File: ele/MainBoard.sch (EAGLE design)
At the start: 120 parts, among them IC1 MCP23017SP, IC2 74HC595D, IC3 74HC595D, X1 POWER_IN, X2 POWER_OUT

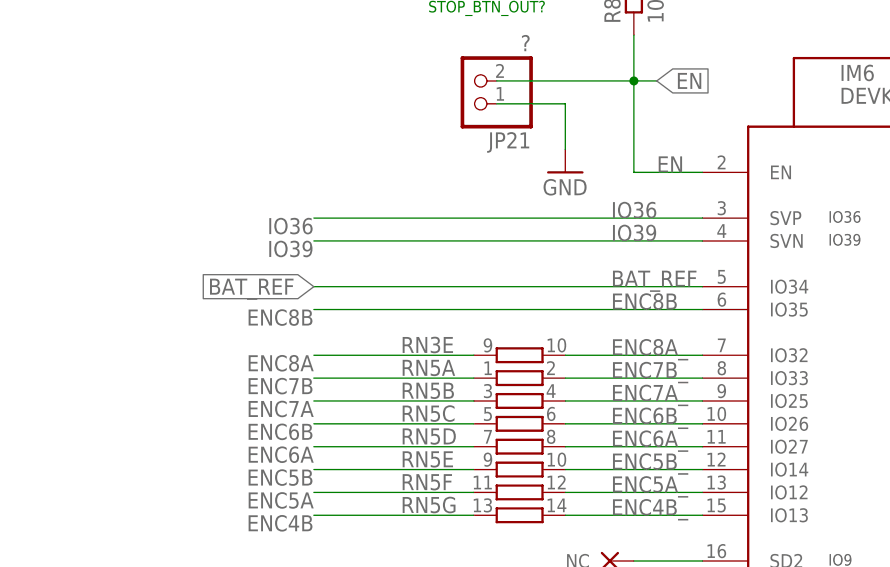
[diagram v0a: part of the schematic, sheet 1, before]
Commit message: ele: Fix typo in net name, move components around
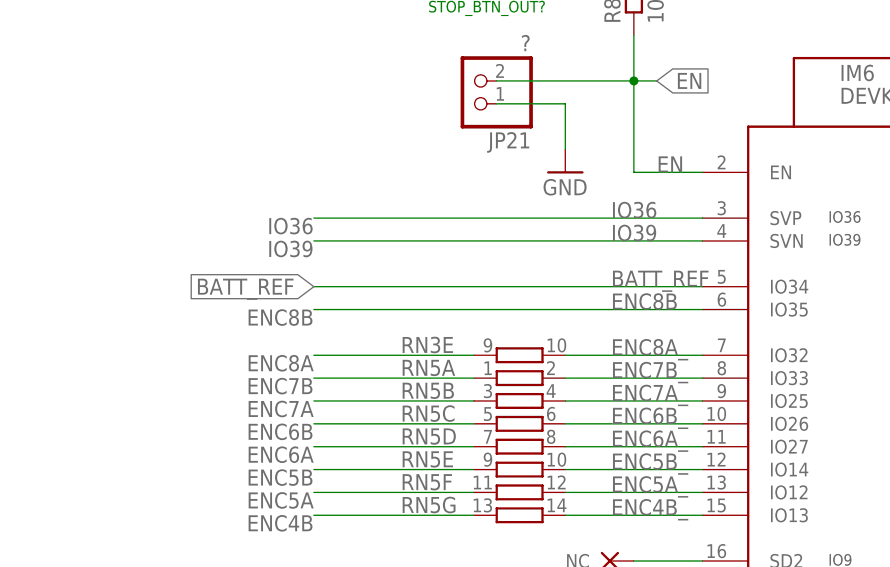
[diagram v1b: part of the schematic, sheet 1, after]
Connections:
- net BATT-ANODE renamed BATT_ANODE2
- net BAT_REF renamed BATT_REF
- removed net BAT_ANODE: Q3.D
- net BATT_ANODE: now also Q3.D
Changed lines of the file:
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@@
 <grid distance="0.1" unitdist="inch" unit="inch" style="lines" multiple="1" display="no" altdistance="0.01" altunitdist="inch" altunit="inch"/>
 <layers>
-<layer number="1" name="Top" color="4" fill="1" visible="yes" active="no"/>
-<layer number="2" name="Route2" color="1" fill="3" visible="yes" active="no"/>
-<layer number="3" name="Route3" color="4" fill="3" visible="yes" active="no"/>
-<layer number="4" name="Route4" color="1" fill="4" visible="yes" active="no"/>
-<layer number="5" name="Route5" color="4" fill="4" visible="yes" active="no"/>
-<layer number="6" name="Route6" color="1" fill="8" visible="yes" active="no"/>
-<layer number="7" name="Route7" color="4" fill="8" visible="yes" active="no"/>
-<layer number="8" name="Route8" color="1" fill="2" visible="yes" active="no"/>
-<layer number="9" name="Route9" color="4" fill="2" visible="yes" active="no"/>
-<layer number="10" name="Route10" color="1" fill="7" visible="yes" active="no"/>
-<layer number="11" name="Route11" color="4" fill="7" visible="yes" active="no"/>
-<layer number="12" name="Route12" color="1" fill="5" visible="yes" active="no"/>
-<layer number="13" name="Route13" color="4" fill="5" visible="yes" active="no"/>
-<layer number="14" name="Route14" color="1" fill="6" visible="yes" active="no"/>
-<layer number="15" name="Route15" color="4" fill="6" visible="yes" active="no"/>
-<layer number="16" name="Bottom" color="1" fill="1" visible="yes" active="no"/>
-<layer number="17" name="Pads" color="2" fill="1" visible="yes" active="no"/>
-<layer number="18" name="Vias" color="2" fill="1" visible="yes" active="no"/>
-<layer number="19" name="Unrouted" color="6" fill="1" visible="yes" active="no"/>
-<layer number="20" name="Dimension" color="24" fill="1" visible="yes" active="no"/>
-<layer number="21" name="tPlace" color="7" fill="1" visible="yes" active="no"/>
-<layer number="22" name="bPlace" color="7" fill="1" visible="yes" active="no"/>
-<layer number="23" name="tOrigins" color="15" fill="1" visible="yes" active="no"/>
-<layer number="24" name="bOrigins" color="15" fill="1" visible="yes" active="no"/>
-<layer number="25" name="tNames" color="7" fill="1" visible="yes" active="no"/>
-<layer number="26" name="bNames" color="7" fill="1" visible="yes" active="no"/>
-<layer number="27" name="tValues" color="7" fill="1" visible="yes" active="no"/>
-<layer number="28" name="bValues" color="7" fill="1" visible="yes" active="no"/>
+<layer number="1" name="Top" color="4" fill="1" visible="no" active="no"/>
+<layer number="2" name="Route2" color="1" fill="3" visible="no" active="no"/>
+<layer number="3" name="Route3" color="4" fill="3" visible="no" active="no"/>
+<layer number="4" name="Route4" color="1" fill="4" visible="no" active="no"/>
+<layer number="5" name="Route5" color="4" fill="4" visible="no" active="no"/>
+<layer number="6" name="Route6" color="1" fill="8" visible="no" active="no"/>
+<layer number="7" name="Route7" color="4" fill="8" visible="no" active="no"/>
+<layer number="8" name="Route8" color="1" fill="2" visible="no" active="no"/>
+<layer number="9" name="Route9" color="4" fill="2" visible="no" active="no"/>
+<layer number="10" name="Route10" color="1" fill="7" visible="no" active="no"/>
+<layer number="11" name="Route11" color="4" fill="7" visible="no" active="no"/>
+<layer number="12" name="Route12" color="1" fill="5" visible="no" active="no"/>
+<layer number="13" name="Route13" color="4" fill="5" visible="no" active="no"/>
+<layer number="14" name="Route14" color="1" fill="6" visible="no" active="no"/>
+<layer number="15" name="Route15" color="4" fill="6" visible="no" active="no"/>
+<layer number="16" name="Bottom" color="1" fill="1" visible="no" active="no"/>
+<layer number="17" name="Pads" color="2" fill="1" visible="no" active="no"/>
+<layer number="18" name="Vias" color="2" fill="1" visible="no" active="no"/>
+<layer number="19" name="Unrouted" color="6" fill="1" visible="no" active="no"/>
+<layer number="20" name="Dimension" color="24" fill="1" visible="no" active="no"/>
+<layer number="21" name="tPlace" color="7" fill="1" visible="no" active="no"/>
+<layer number="22" name="bPlace" color="7" fill="1" visible="no" active="no"/>
+<layer number="23" name="tOrigins" color="15" fill="1" visible="no" active="no"/>
+<layer number="24" name="bOrigins" color="15" fill="1" visible="no" active="no"/>
+<layer number="25" name="tNames" color="7" fill="1" visible="no" active="no"/>
+<layer number="26" name="bNames" color="7" fill="1" visible="no" active="no"/>
+<layer number="27" name="tValues" color="7" fill="1" visible="no" active="no"/>
+<layer number="28" name="bValues" color="7" fill="1" visible="no" active="no"/>
 <layer number="29" name="tStop" color="7" fill="3" visible="no" active="no"/>
 <layer number="30" name="bStop" color="7" fill="6" visible="no" active="no"/>
@@
 <layer number="35" name="tGlue" color="7" fill="4" visible="no" active="no"/>
 <layer number="36" name="bGlue" color="7" fill="5" visible="no" active="no"/>
-<layer number="37" name="tTest" color="7" fill="1" visible="yes" active="no"/>
-<layer number="38" name="bTest" color="7" fill="1" visible="yes" active="no"/>
+<layer number="37" name="tTest" color="7" fill="1" visible="no" active="no"/>
+<layer number="38" name="bTest" color="7" fill="1" visible="no" active="no"/>
 <layer number="39" name="tKeepout" color="4" fill="11" visible="no" active="no"/>
 <layer number="40" name="bKeepout" color="1" fill="11" visible="no" active="no"/>
@@
 <layer number="44" name="Drills" color="7" fill="1" visible="no" active="no"/>
 <layer number="45" name="Holes" color="7" fill="1" visible="no" active="no"/>
-<layer number="46" name="Milling" color="3" fill="1" visible="yes" active="no"/>
-<layer number="47" name="Measures" color="7" fill="1" visible="yes" active="no"/>
-<layer number="48" name="Document" color="7" fill="1" visible="yes" active="no"/>
-<layer number="49" name="Reference" color="7" fill="1" visible="yes" active="no"/>
-<layer number="50" name="dxf" color="7" fill="1" visible="yes" active="no"/>
-<layer number="51" name="tDocu" color="7" fill="1" visible="yes" active="no"/>
-<layer number="52" name="bDocu" color="7" fill="1" visible="yes" active="no"/>
-<layer number="53" name="tGND_GNDA" color="7" fill="9" visible="yes" active="no"/>
-<layer number="54" name="bGND_GNDA" color="1" fill="9" visible="yes" active="no"/>
-<layer number="55" name="tPotisk" color="7" fill="1" visible="yes" active="no"/>
-<layer number="56" name="wert" color="7" fill="1" visible="yes" active="no"/>
-<layer number="57" name="tCAD" color="7" fill="1" visible="yes" active="no"/>
-<layer number="58" name="bNC" color="7" fill="1" visible="yes" active="no"/>
-<layer number="59" name="tCarbon" color="7" fill="1" visible="yes" active="no"/>
-<layer number="60" name="bCarbon" color="7" fill="1" visible="yes" active="no"/>
-<layer number="61" name="stand" color="7" fill="1" visible="yes" active="no"/>
+<layer number="46" name="Milling" color="3" fill="1" visible="no" active="no"/>
+<layer number="47" name="Measures" color="7" fill="1" visible="no" active="no"/>
+<layer number="48" name="Document" color="7" fill="1" visible="no" active="no"/>
+<layer number="49" name="Reference" color="7" fill="1" visible="no" active="no"/>
+<layer number="50" name="dxf" color="7" fill="1" visible="no" active="no"/>
+<layer number="51" name="tDocu" color="7" fill="1" visible="no" active="no"/>
+<layer number="52" name="bDocu" color="7" fill="1" visible="no" active="no"/>
+<layer number="53" name="tGND_GNDA" color="7" fill="9" visible="no" active="no"/>
+<layer number="54" name="bGND_GNDA" color="1" fill="9" visible="no" active="no"/>
+<layer number="55" name="tPotisk" color="7" fill="1" visible="no" active="no"/>
+<layer number="56" name="wert" color="7" fill="1" visible="no" active="no"/>
+<layer number="57" name="tCAD" color="7" fill="1" visible="no" active="no"/>
+<layer number="58" name="bNC" color="7" fill="1" visible="no" active="no"/>
+<layer number="59" name="tCarbon" color="7" fill="1" visible="no" active="no"/>
+<layer number="60" name="bCarbon" color="7" fill="1" visible="no" active="no"/>
+<layer number="61" name="stand" color="7" fill="1" visible="no" active="no"/>
 <layer number="88" name="SimResults" color="9" fill="1" visible="yes" active="yes"/>
 <layer number="89" name="SimProbes" color="9" fill="1" visible="yes" active="yes"/>
@@
 </segment>
 </net>
-<net name="BAT_REF" class="0">
+<net name="BATT_REF" class="0">
 <segment>
 <label x="205.74" y="200.66" size="1.778" layer="95" rot="R180" xref="yes"/>
@@
 </segment>
 </net>
-<net name="BAT_REF" class="0">
+<net name="BATT_REF" class="0">
 <segment>
 <pinref part="R3" gate="G$1" pin="2"/>
@@
 <label x="127" y="193.04" size="1.778" layer="95"/>
 </segment>
+<segment>
+<pinref part="Q3" gate="G$1" pin="D"/>
+<wire x1="15.24" y1="182.88" x2="15.24" y2="177.8" width="0.1524" layer="91"/>
+<label x="15.24" y="177.8" size="1.778" layer="95" rot="R270"/>
+</segment>
 </net>
 <net name="N$4" class="0">
@@
 </segment>
 </net>
-<net name="BATT-ANODE" class="0">
+<net name="BATT_ANODE2" class="0">
 <segment>
 <pinref part="Q1" gate="G$1" pin="S"/>
@@
 </segment>
 </net>
-<net name="BAT_ANODE" class="0">
-<segment>
-<pinref part="Q3" gate="G$1" pin="D"/>
-<wire x1="15.24" y1="182.88" x2="15.24" y2="177.8" width="0.1524" layer="91"/>
-<label x="15.24" y="177.8" size="1.778" layer="95" rot="R270"/>
-</segment>
-</net>

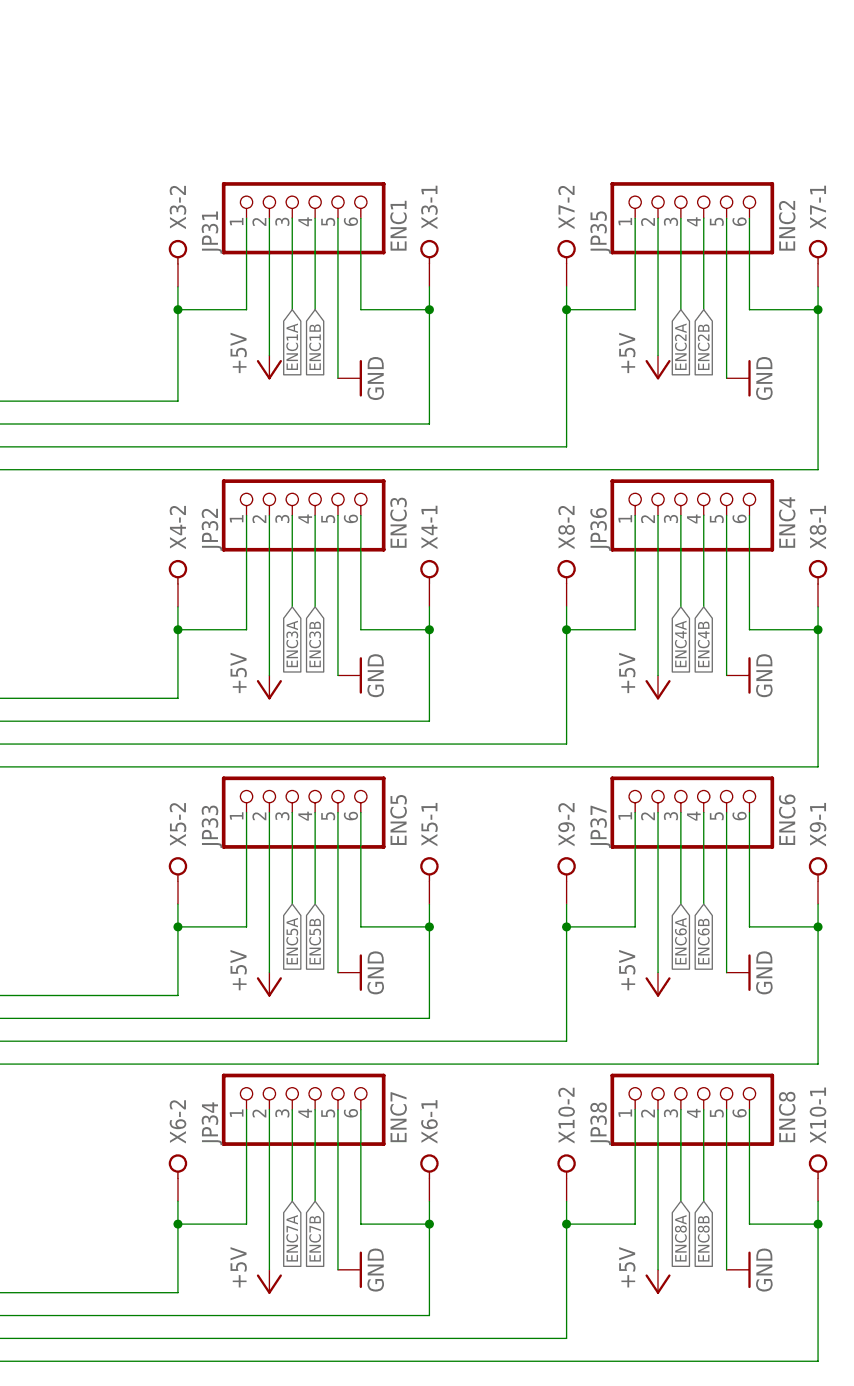
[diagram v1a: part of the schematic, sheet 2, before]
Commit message: ele: Create main power polygons, flip power connectors
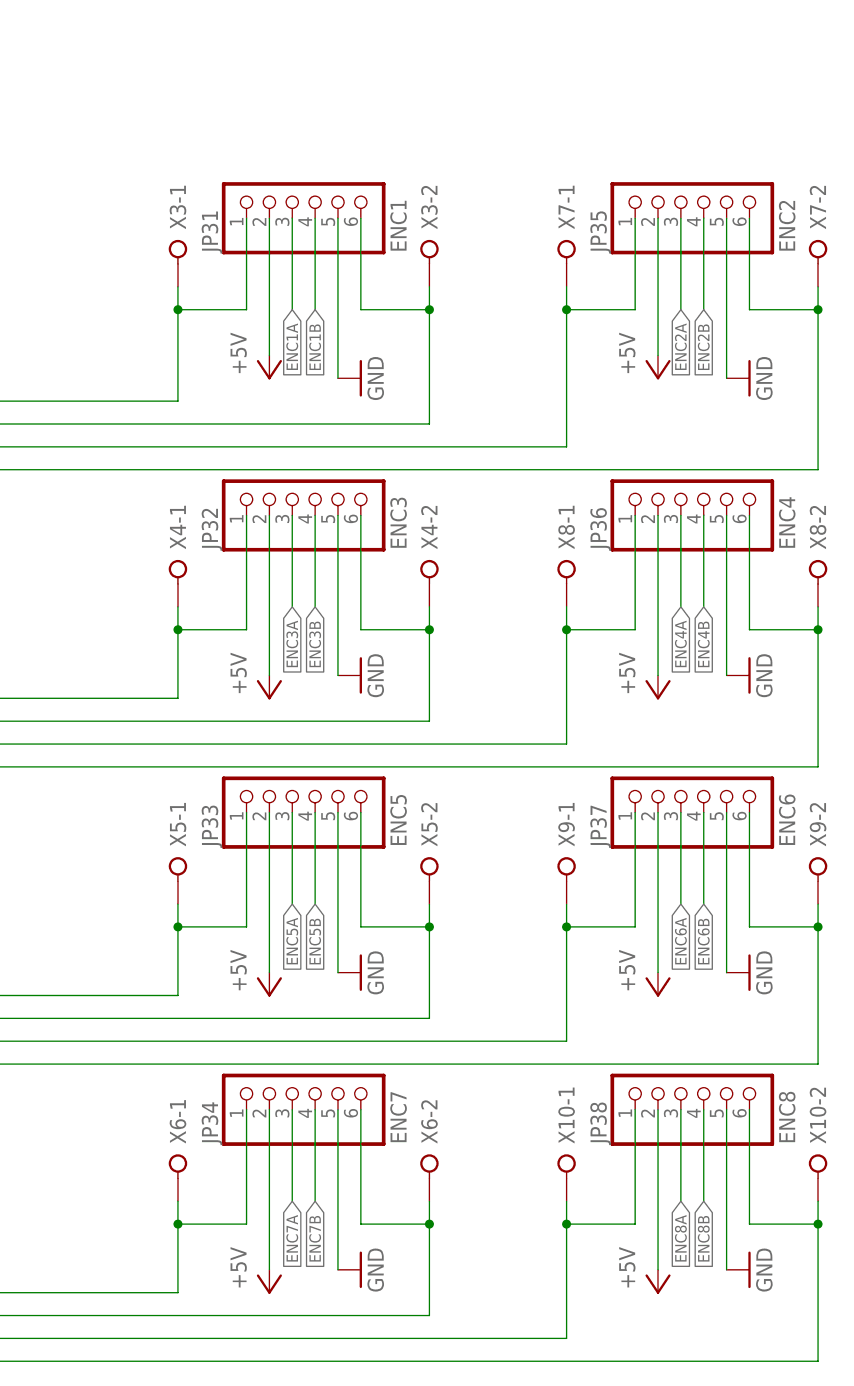
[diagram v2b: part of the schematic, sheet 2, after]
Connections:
- net IM10_O1: now also X6-1.KL; no longer X6-2.KL
- net IM10_O2: now also X6-2.KL; no longer X6-1.KL
- net IM10_O3: now also X10-1.KL; no longer X10-2.KL
- net IM10_O4: now also X10-2.KL; no longer X10-1.KL
- net IM7_O1: now also X3-1.KL; no longer X3-2.KL
- net IM7_O2: now also X3-2.KL; no longer X3-1.KL
- net IM7_O3: now also X7-1.KL; no longer X7-2.KL
- net IM7_O4: now also X7-2.KL; no longer X7-1.KL
- net IM8_O1: now also X4-1.KL; no longer X4-2.KL
- net IM8_O2: now also X4-2.KL; no longer X4-1.KL
- net IM8_O3: now also X8-1.KL; no longer X8-2.KL
- net IM8_O4: now also X8-2.KL; no longer X8-1.KL
- net IM9_O1: now also X5-1.KL; no longer X5-2.KL
- net IM9_O2: now also X5-2.KL; no longer X5-1.KL
- net IM9_O3: now also X9-1.KL; no longer X9-2.KL
- net IM9_O4: now also X9-2.KL; no longer X9-1.KL
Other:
- moved on the sheet: X10-1, X10-2, X3-1, X3-2, X4-1, X4-2, X5-1, X5-2, X6-1, X6-2, X7-1, X7-2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

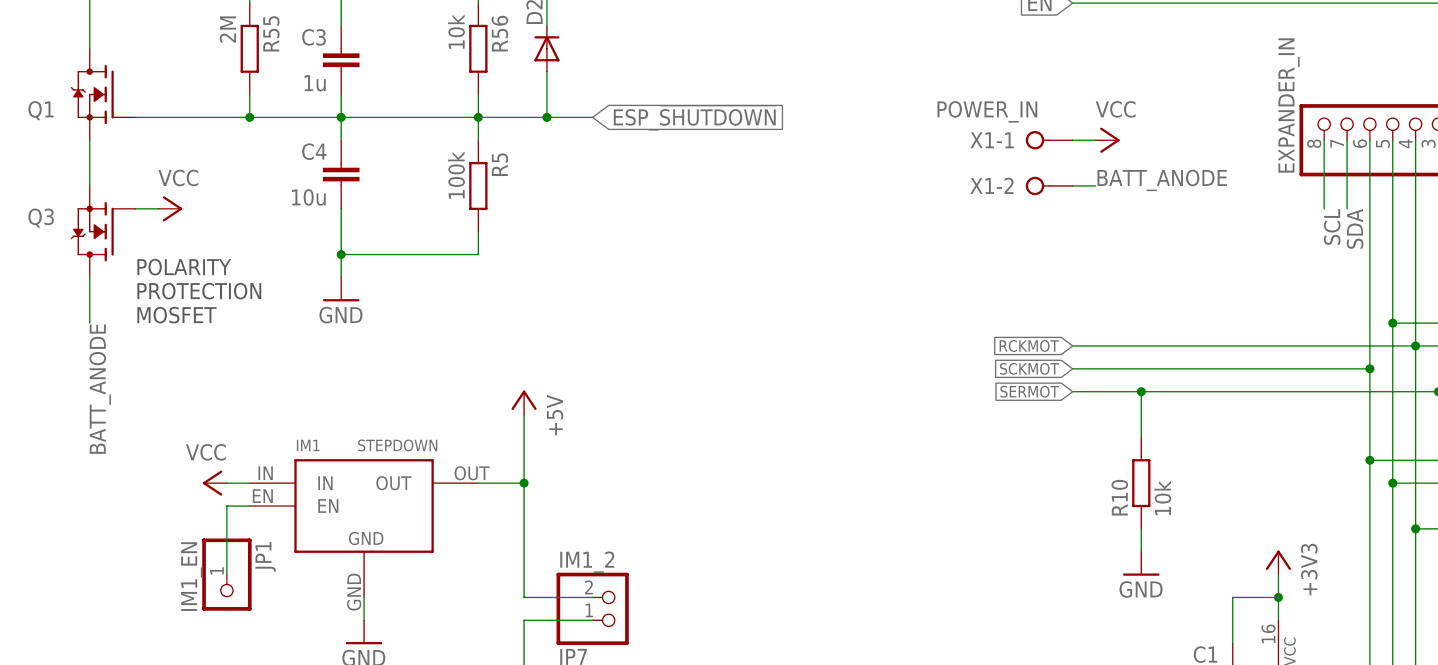
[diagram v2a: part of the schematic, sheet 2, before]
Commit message: ele: Route some signals, make room for large currents
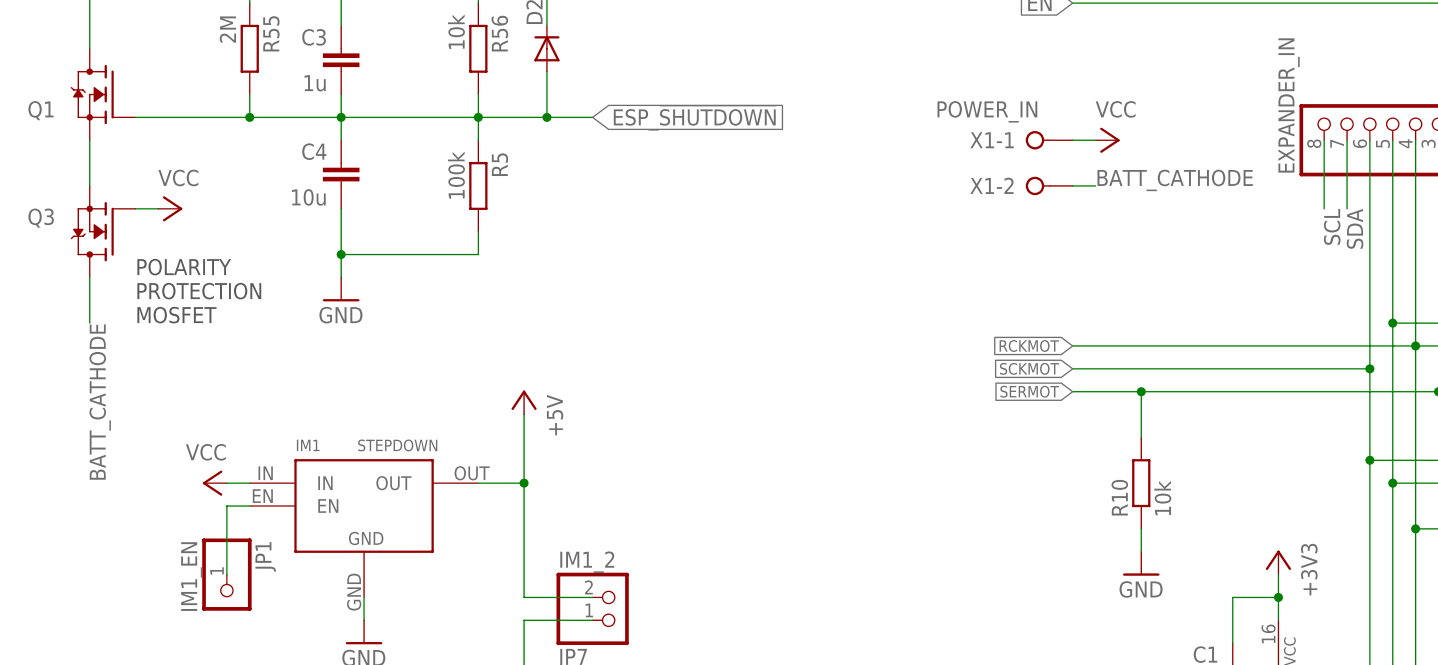
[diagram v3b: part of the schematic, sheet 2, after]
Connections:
- net BATT_ANODE renamed BATT_CATHODE
- net BATT_ANODE2 renamed BATT_CATHODE2
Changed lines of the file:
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@@
 </segment>
 </net>
-<net name="BATT_ANODE" class="0">
+<net name="BATT_CATHODE" class="0">
 <segment>
 <pinref part="X1" gate="-2" pin="KL"/>
@@
 </segment>
 </net>
-<net name="BATT_ANODE2" class="0">
+<net name="BATT_CATHODE2" class="0">
 <segment>
 <pinref part="Q1" gate="G$1" pin="S"/>
